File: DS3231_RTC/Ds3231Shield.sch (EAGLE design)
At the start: 5 parts

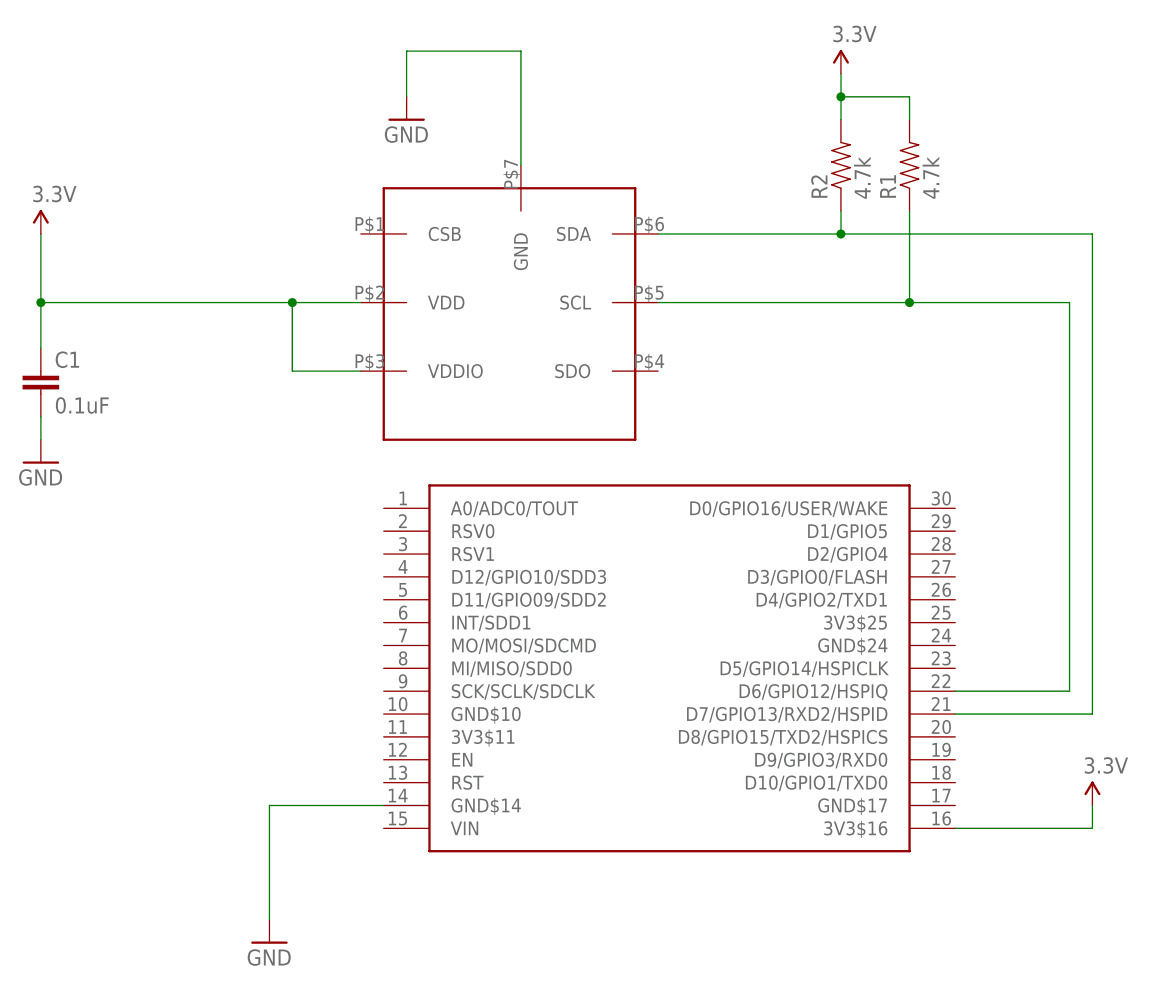
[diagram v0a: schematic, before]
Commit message: Updated BMP180 symbol Removed BMP085 shield (redundant) Added DS3231 RTC Shield Added LTC2495 ADC Shield Added chip data sheets for each shield
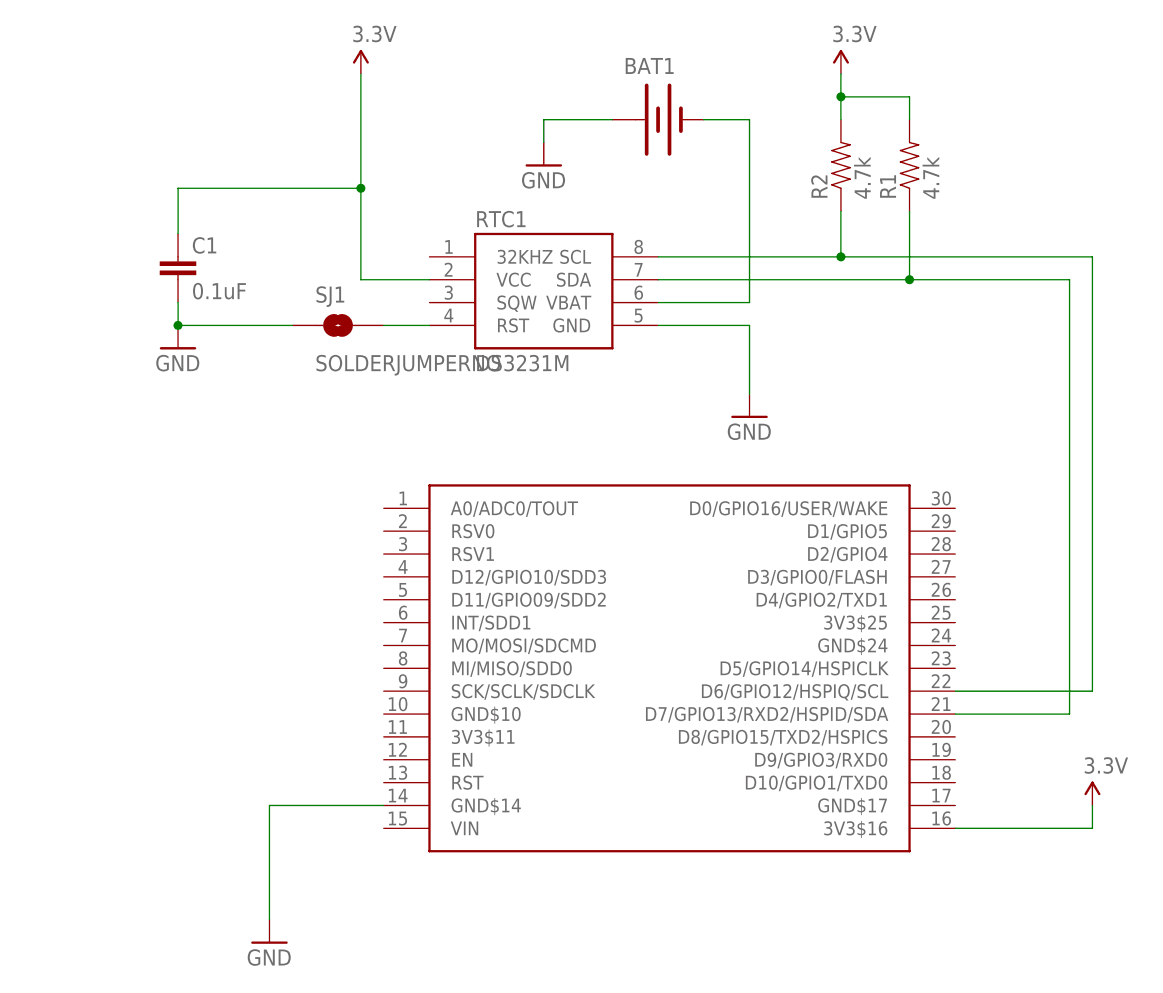
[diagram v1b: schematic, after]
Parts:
- removed U$3: BMP180, NerduinoShieldLib:BMP180
- added BAT1: (no value), SparkFun-Electromechanical:BATTERY12MM
- added RTC1: DS3231M, SparkFun-DigitalIC:DS3231M
- added SJ1: SOLDERJUMPERNO, SparkFun:SOLDERJUMPERNO
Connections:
- new net N$1: BAT1.-, RTC1.VBAT
- new net N$4: RTC1.RST, SJ1.2
- net 3.3V: now also RTC1.VCC; no longer U$3.VDD, U$3.VDDIO
- net GND: now also BAT1.+, RTC1.GND, SJ1.1; no longer U$3.GND
- net N$2: now also RTC1.SCL, U$1.D6/GPIO12/HSPIQ/SCL; no longer U$1.D7/GPIO13/RXD2/HSPID, U$3.SDA
- net N$3: now also RTC1.SDA, U$1.D7/GPIO13/RXD2/HSPID/SDA; no longer U$1.D6/GPIO12/HSPIQ, U$3.SCL
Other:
- moved on the sheet: C1

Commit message: Added OLED Shield Added LiPo Battery Charger Shield Updated outlines of all shields to match the cutout of the nodemcu board
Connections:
- net GND: now also U$1.GND$10, U$1.GND$17, U$1.GND$24
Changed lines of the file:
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@@
 <part name="GND4" library="SparkFun" deviceset="GND" device=""/>
 <part name="SJ1" library="SparkFun" deviceset="SOLDERJUMPER" device="NO"/>
+<part name="GND5" library="SparkFun" deviceset="GND" device=""/>
 </parts>
 <sheets>
@@
 <instance part="GND4" gate="1" x="25.4" y="104.14"/>
 <instance part="SJ1" gate="1" x="2.54" y="86.36"/>
+<instance part="GND5" gate="1" x="76.2" y="17.78"/>
 </instances>
 <busses>
@@
 <wire x1="7.62" y1="33.02" x2="-5.08" y2="33.02" width="0.1524" layer="91"/>
 <wire x1="-5.08" y1="33.02" x2="-5.08" y2="20.32" width="0.1524" layer="91"/>
+<pinref part="U$1" gate="G$1" pin="GND$10"/>
+<wire x1="7.62" y1="43.18" x2="-5.08" y2="43.18" width="0.1524" layer="91"/>
+<wire x1="-5.08" y1="43.18" x2="-5.08" y2="33.02" width="0.1524" layer="91"/>
+<junction x="-5.08" y="33.02"/>
 </segment>
 <segment>
@@
 <wire x1="25.4" y1="109.22" x2="25.4" y2="106.68" width="0.1524" layer="91"/>
 </segment>
+<segment>
+<pinref part="U$1" gate="G$1" pin="GND$24"/>
+<pinref part="GND5" gate="1" pin="GND"/>
+<wire x1="71.12" y1="50.8" x2="76.2" y2="50.8" width="0.1524" layer="91"/>
+<wire x1="76.2" y1="50.8" x2="76.2" y2="33.02" width="0.1524" layer="91"/>
+<pinref part="U$1" gate="G$1" pin="GND$17"/>
+<wire x1="76.2" y1="33.02" x2="76.2" y2="20.32" width="0.1524" layer="91"/>
+<wire x1="71.12" y1="33.02" x2="76.2" y2="33.02" width="0.1524" layer="91"/>
+<junction x="76.2" y="33.02"/>
+</segment>
 </net>

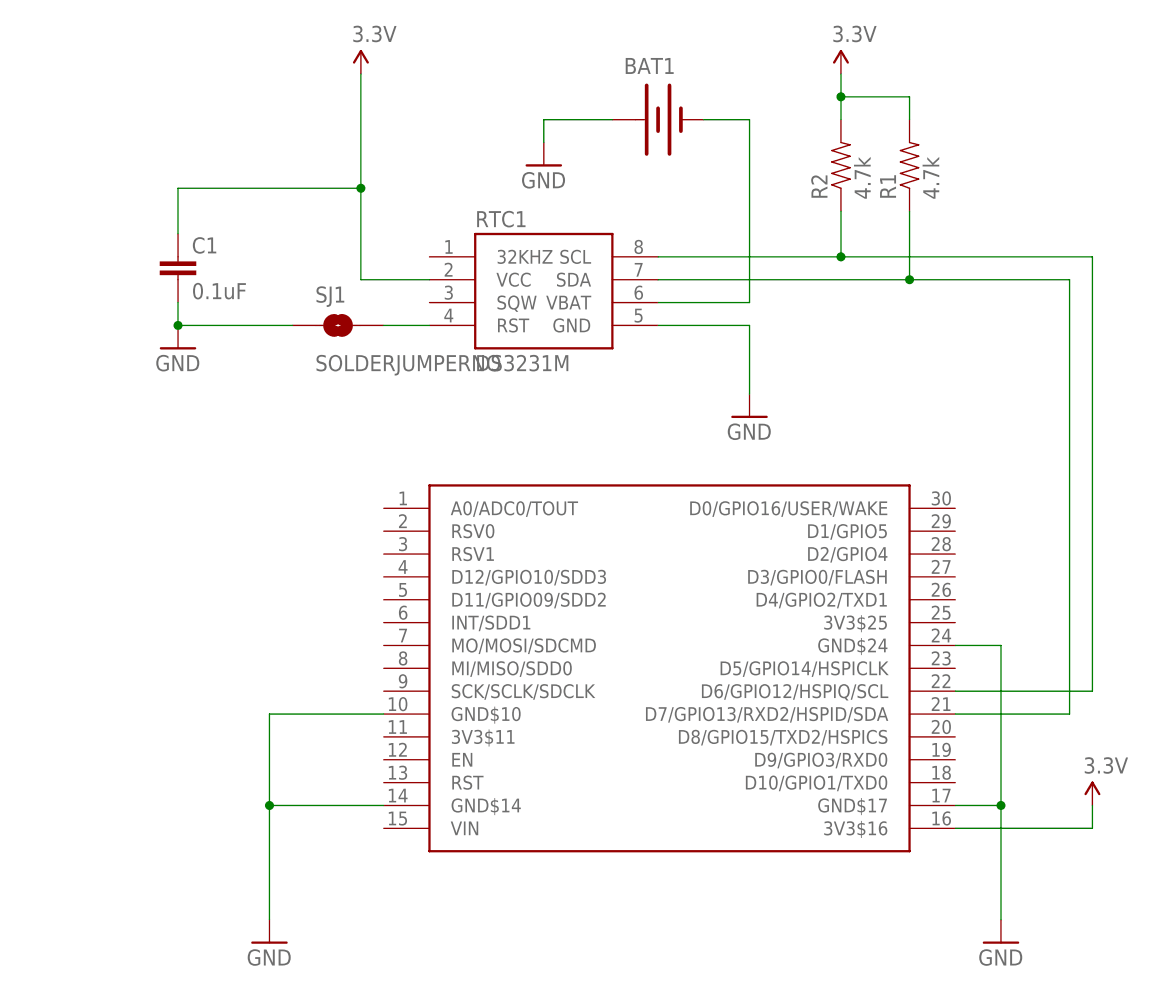
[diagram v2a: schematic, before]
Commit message: Updated the i2c pins to all shields to use d11/d12  as these pins will have dual use with the upcoming wifimcu Added FM24W256  Fram shield Added X95840 Digital potentiometer Shield Added AD5696 DAC Shield
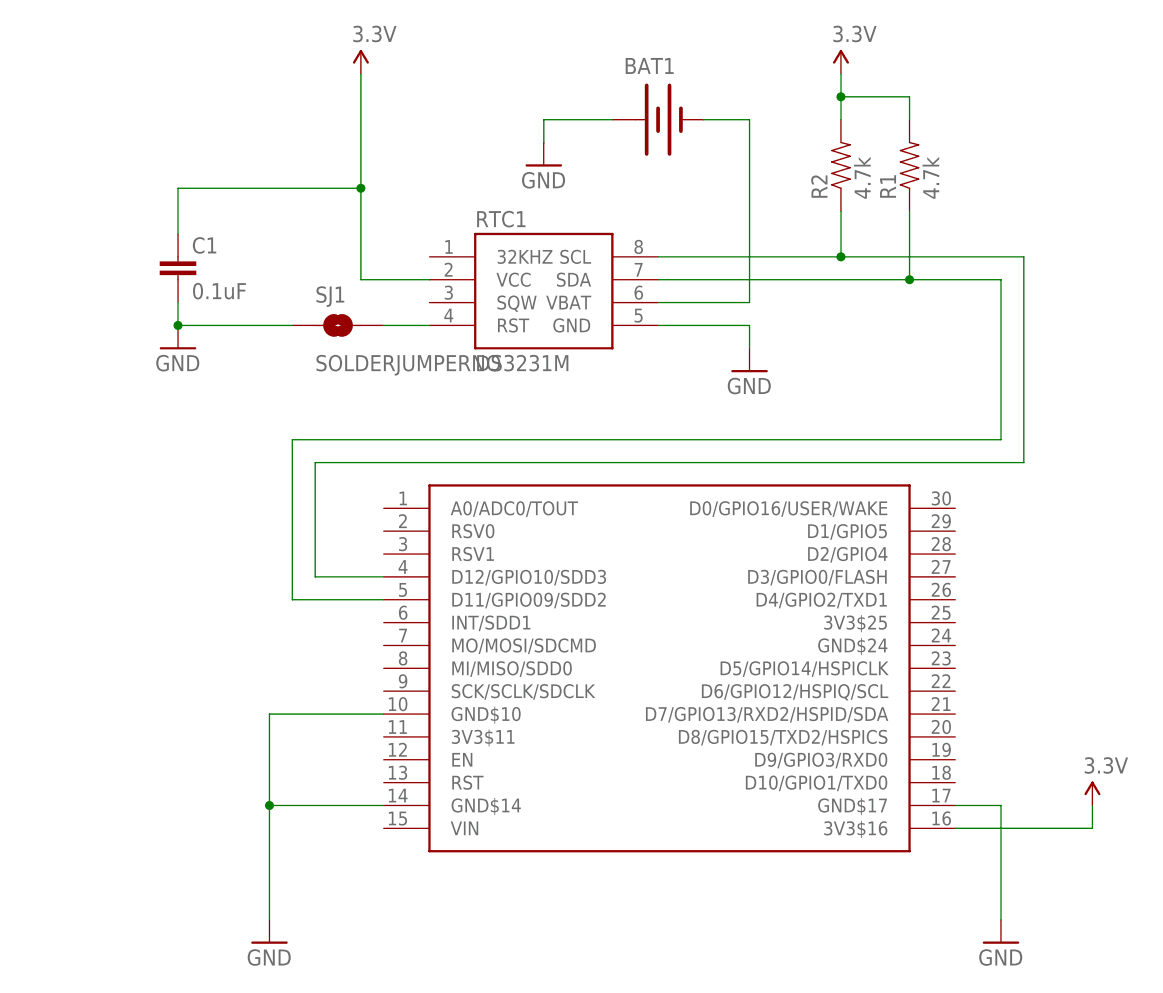
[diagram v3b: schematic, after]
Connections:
- net GND: no longer U$1.GND$24
- net N$2: now also U$1.D12/GPIO10/SDD3; no longer U$1.D6/GPIO12/HSPIQ/SCL
- net N$3: now also U$1.D11/GPIO09/SDD2; no longer U$1.D7/GPIO13/RXD2/HSPID/SDA
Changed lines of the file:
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@@
 <instance part="P+3" gate="G$1" x="58.42" y="114.3"/>
 <instance part="GND2" gate="1" x="-15.24" y="83.82"/>
-<instance part="GND3" gate="1" x="48.26" y="76.2"/>
+<instance part="GND3" gate="1" x="48.26" y="81.28"/>
 <instance part="RTC1" gate="G$1" x="25.4" y="88.9"/>
 <instance part="BAT1" gate="G$1" x="38.1" y="109.22"/>
@@
 <segment>
 <pinref part="GND3" gate="1" pin="GND"/>
-<wire x1="48.26" y1="86.36" x2="48.26" y2="78.74" width="0.1524" layer="91"/>
+<wire x1="48.26" y1="86.36" x2="48.26" y2="83.82" width="0.1524" layer="91"/>
 <pinref part="RTC1" gate="G$1" pin="GND"/>
 <wire x1="48.26" y1="86.36" x2="38.1" y2="86.36" width="0.1524" layer="91"/>
@@
 </segment>
 <segment>
-<pinref part="U$1" gate="G$1" pin="GND$24"/>
 <pinref part="GND5" gate="1" pin="GND"/>
-<wire x1="71.12" y1="50.8" x2="76.2" y2="50.8" width="0.1524" layer="91"/>
-<wire x1="76.2" y1="50.8" x2="76.2" y2="33.02" width="0.1524" layer="91"/>
 <pinref part="U$1" gate="G$1" pin="GND$17"/>
 <wire x1="76.2" y1="33.02" x2="76.2" y2="20.32" width="0.1524" layer="91"/>
 <wire x1="71.12" y1="33.02" x2="76.2" y2="33.02" width="0.1524" layer="91"/>
-<junction x="76.2" y="33.02"/>
 </segment>
 </net>
@@
 <wire x1="38.1" y1="93.98" x2="58.42" y2="93.98" width="0.1524" layer="91"/>
 <wire x1="58.42" y1="93.98" x2="58.42" y2="99.06" width="0.1524" layer="91"/>
-<wire x1="58.42" y1="93.98" x2="86.36" y2="93.98" width="0.1524" layer="91"/>
+<wire x1="58.42" y1="93.98" x2="78.74" y2="93.98" width="0.1524" layer="91"/>
 <junction x="58.42" y="93.98"/>
-<pinref part="U$1" gate="G$1" pin="D6/GPIO12/HSPIQ/SCL"/>
-<wire x1="71.12" y1="45.72" x2="86.36" y2="45.72" width="0.1524" layer="91"/>
-<wire x1="86.36" y1="45.72" x2="86.36" y2="93.98" width="0.1524" layer="91"/>
 <pinref part="RTC1" gate="G$1" pin="SCL"/>
+<pinref part="U$1" gate="G$1" pin="D12/GPIO10/SDD3"/>
+<wire x1="7.62" y1="58.42" x2="0" y2="58.42" width="0.1524" layer="91"/>
+<wire x1="0" y1="58.42" x2="0" y2="71.12" width="0.1524" layer="91"/>
+<wire x1="0" y1="71.12" x2="78.74" y2="71.12" width="0.1524" layer="91"/>
+<wire x1="78.74" y1="71.12" x2="78.74" y2="93.98" width="0.1524" layer="91"/>
 </segment>
 </net>
@@
 <wire x1="38.1" y1="91.44" x2="66.04" y2="91.44" width="0.1524" layer="91"/>
 <wire x1="66.04" y1="91.44" x2="66.04" y2="99.06" width="0.1524" layer="91"/>
-<wire x1="66.04" y1="91.44" x2="83.82" y2="91.44" width="0.1524" layer="91"/>
-<wire x1="83.82" y1="91.44" x2="83.82" y2="43.18" width="0.1524" layer="91"/>
+<wire x1="66.04" y1="91.44" x2="76.2" y2="91.44" width="0.1524" layer="91"/>
 <junction x="66.04" y="91.44"/>
-<pinref part="U$1" gate="G$1" pin="D7/GPIO13/RXD2/HSPID/SDA"/>
-<wire x1="71.12" y1="43.18" x2="83.82" y2="43.18" width="0.1524" layer="91"/>
 <pinref part="RTC1" gate="G$1" pin="SDA"/>
+<pinref part="U$1" gate="G$1" pin="D11/GPIO09/SDD2"/>
+<wire x1="7.62" y1="55.88" x2="-2.54" y2="55.88" width="0.1524" layer="91"/>
+<wire x1="-2.54" y1="55.88" x2="-2.54" y2="73.66" width="0.1524" layer="91"/>
+<wire x1="-2.54" y1="73.66" x2="76.2" y2="73.66" width="0.1524" layer="91"/>
+<wire x1="76.2" y1="73.66" x2="76.2" y2="91.44" width="0.1524" layer="91"/>
 </segment>
 </net>
